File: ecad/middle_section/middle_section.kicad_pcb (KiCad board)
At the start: 2 copper layers, 12 parts, among them U1 ADS7830, U2 LM4040DBZ-3

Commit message: [WIP]
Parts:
- added J1: JST SH, Connector_JST:JST_SH_BM04B-SRSS-TB_1x04-1MP_P1.00mm_Vertical, B.Cu at (99.5, 125.6)
- added JP1: ~, Jumper:SolderJumper-3_P1.3mm_Open_RoundedPad1.0x1.5mm, B.Cu at (109.3, 129.3)
- added JP2: ~, Jumper:SolderJumper-3_P1.3mm_Open_RoundedPad1.0x1.5mm, B.Cu at (109.3, 126.8)
- C1, C3: value C_Polarized -> 2u2; footprint Capacitor_SMD:CP_Elec_4x5.7 -> Capacitor_SMD:C_0805_2012Metric; moved to B.Cu
- C2, C4: value C -> 100n; moved to B.Cu
- R1: value R -> 100; moved to B.Cu
- U1, U2: moved to B.Cu
- moved RV1 60.8 mm to (100.0, 100.0), turned to 90 degrees
- moved RV2 38.5 mm to (119.0, 100.0), turned to 90 degrees
- moved RV5 30.5 mm to (176.0, 100.0), turned to 90 degrees
- moved C1 27.8 mm to (113.2, 120.5)
- moved R1 25.1 mm to (113.2, 126.3), turned to 0 degrees
- moved C2 22.9 mm to (113.2, 118.7)
- moved C3 22.6 mm to (103.2, 121.6), turned to 90 degrees
- moved C4 22.1 mm to (105.0, 121.8), turned to 90 degrees
- moved U2 21.1 mm to (113.3, 123.5), turned to -90 degrees
- moved U1 20.9 mm to (108.6, 119.4), turned to -90 degrees
- moved RV3 16.8 mm to (138.0, 100.0), turned to 90 degrees
- moved RV4 9.94 mm to (157.0, 100.0), turned to 90 degrees
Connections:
- U1 pad 12: unconnected-(U1-A0-Pad12) -> /A1
- U1 pad 13: unconnected-(U1-A1-Pad13) -> /A0
- U1 pad 14: unconnected-(U1-SCL-Pad14) -> /SCK
- U1 pad 15: unconnected-(U1-SDA-Pad15) -> /SDA
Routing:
- net /SCK: track 0.00 -> 9.33 mm
- net +3V3: track 0.00 -> 8.92 mm
- net /SDA: track 0.00 -> 7.95 mm
- net /A0: track 0.00 -> 7.50 mm, vias 0 -> 2
- net +3V0: track 0.00 -> 7.37 mm
- net GND: track 0.00 -> 7.19 mm
- net /A1: track 0.00 -> 4.71 mm
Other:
- board outline added: 100 x 78 mm

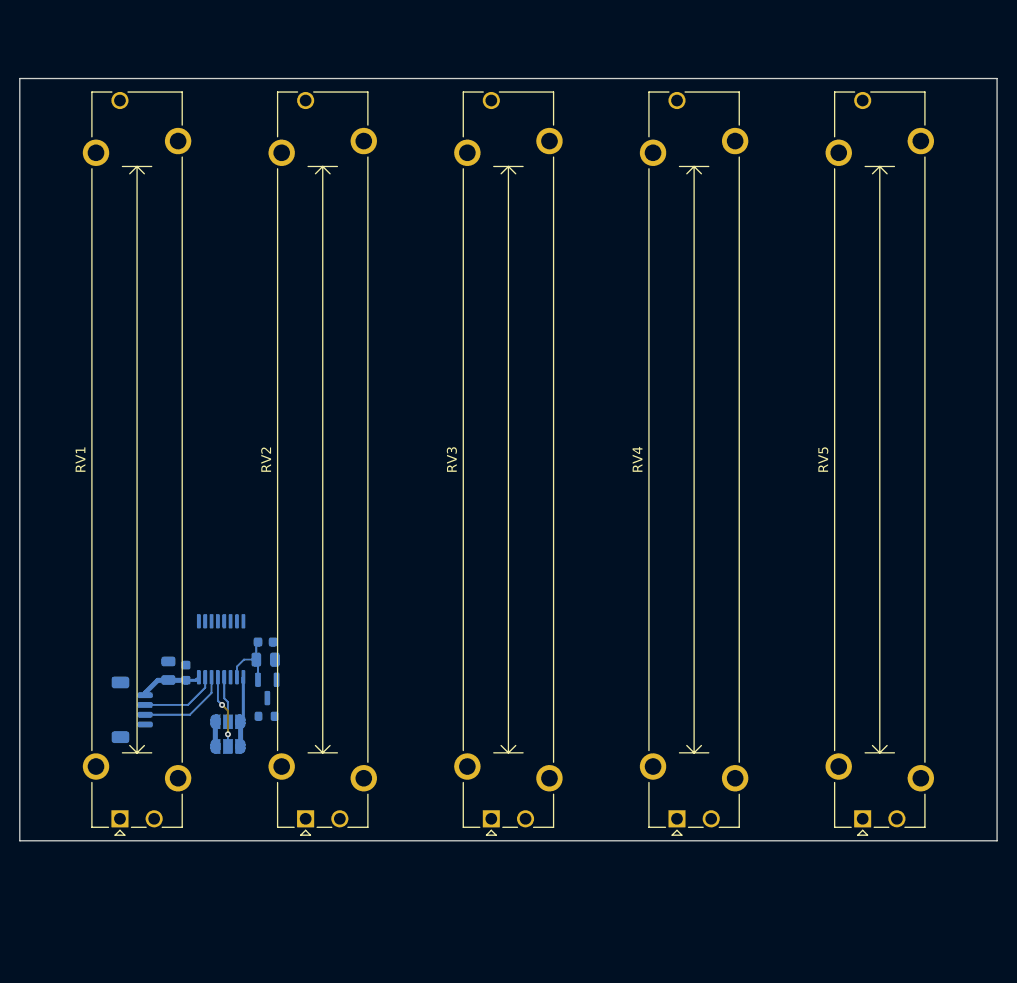
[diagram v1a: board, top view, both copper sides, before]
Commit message: Finishes up Middle Section
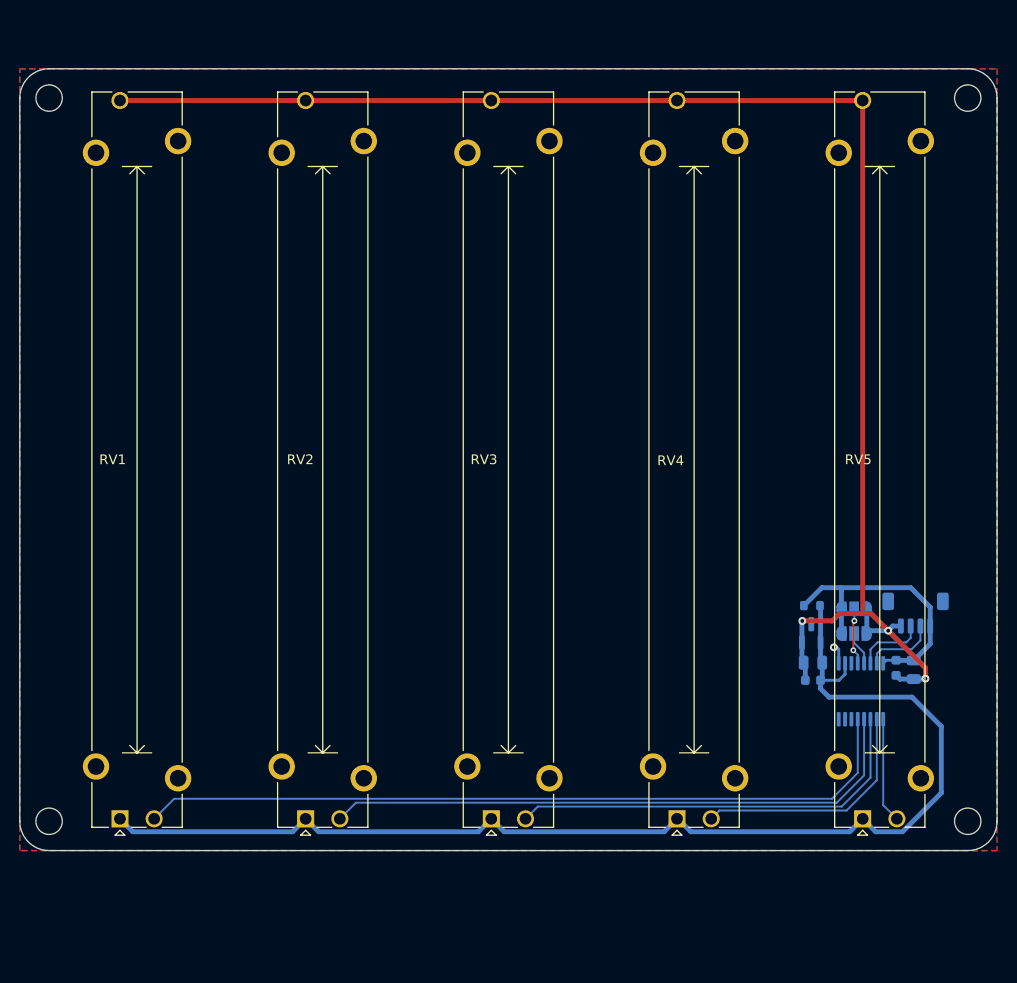
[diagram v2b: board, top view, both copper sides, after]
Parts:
- added REF**: MountingHole_2.7mm_M2.5, MountingHole:MountingHole_2.7mm_M2.5, F.Cu at (185.0, 63.0)
- added REF**: MountingHole_2.7mm_M2.5, MountingHole:MountingHole_2.7mm_M2.5, F.Cu at (91.0, 63.0)
- added REF**: MountingHole_2.7mm_M2.5, MountingHole:MountingHole_2.7mm_M2.5, F.Cu at (185.0, 137.0)
- added REF**: MountingHole_2.7mm_M2.5, MountingHole:MountingHole_2.7mm_M2.5, F.Cu at (91.0, 137.0)
- moved J1 80.8 mm to (179.7, 115.7), turned to 180 degrees
- moved C3 76.3 mm to (179.5, 121.5), turned to -90 degrees
- moved C4 72.7 mm to (177.7, 121.3), turned to -90 degrees
- moved U1 65.6 mm to (174.1, 123.7), turned to 90 degrees
- moved JP1 65.1 mm to (173.4, 117.8)
- moved JP2 65.1 mm to (173.4, 115.3)
- moved R1 56.9 mm to (169.1, 114.9)
- moved C2 56.1 mm to (169.2, 122.6), turned to 180 degrees
- moved C1 56.0 mm to (169.2, 120.8), turned to 180 degrees
- moved U2 55.9 mm to (169.0, 117.8), turned to 90 degrees
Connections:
- U1 pad 1: /CH0 -> /CH4
- U1 pad 2: /CH1 -> /CH3
- U1 pad 4: /CH3 -> /CH1
- U1 pad 5: /CH4 -> /CH0
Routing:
- net GND: track 7.19 -> 162.6 mm, vias 0 -> 4
- net +3V0: track 7.37 -> 124.0 mm
- net /CH0: track 0.00 -> 79.4 mm
- net /CH1: track 0.00 -> 61.2 mm
- net /CH2: track 0.00 -> 43.0 mm
- net /CH3: track 0.00 -> 24.8 mm
- net +3V3: track 8.92 -> 28.7 mm
- net /CH4: track 0.00 -> 10.8 mm
- net /A0: track 7.50 -> 3.47 mm, vias 2 -> 0
- net /SCK: track 9.33 -> 7.24 mm
- net /A1: track 4.71 -> 5.82 mm, vias 0 -> 2
- added copper zone on B.Cu, net GND
- added copper zone on F.Cu, net GND
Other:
- board size 100 x 78 mm -> 100 x 80 mm
- board text added: "Addr"
- board text added: "ON"

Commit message: Updates boards
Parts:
- added R2: 100, Resistor_SMD:R_0603_1608Metric, B.Cu at (169.1, 113.4)
- J1: footprint Connector_JST:JST_SH_BM04B-SRSS-TB_1x04-1MP_P1.00mm_Vertical -> woodpecker:JST_SH_BM04B-SRSS-TB_1x04-1MP_P1.00mm_Vertical
- JP1, JP2: footprint Jumper:SolderJumper-3_P1.3mm_Open_RoundedPad1.0x1.5mm -> Jumper:SolderJumper-3_P2.0mm_Open_TrianglePad1.0x1.5mm; moved to F.Cu
- moved JP1 11.7 mm to (167.8, 107.5), turned to -90 degrees
- moved JP2 11.2 mm to (165.3, 107.5), turned to -90 degrees
- moved J1 3.66 mm to (176.0, 115.7)
- moved R1 0.06 mm to (169.1, 114.9)
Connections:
- JP1 pad 1: +3V3 -> Net-(JP1-A)
- JP2 pad 1: +3V3 -> Net-(JP1-A)
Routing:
- net Net-(JP1-A): track 0.00 -> 17.6 mm, vias 0 -> 1
- net /A1: track 5.82 -> 20.4 mm, vias 2 -> 1
- net /A0: track 3.47 -> 16.9 mm, vias 0 -> 1
- net +3V3: track 28.7 -> 22.4 mm
- net /SDA: track 7.48 -> 4.15 mm
- net /SCK: track 7.24 -> 4.00 mm
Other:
- board text added: "↑ON"
- board text removed: "ON"

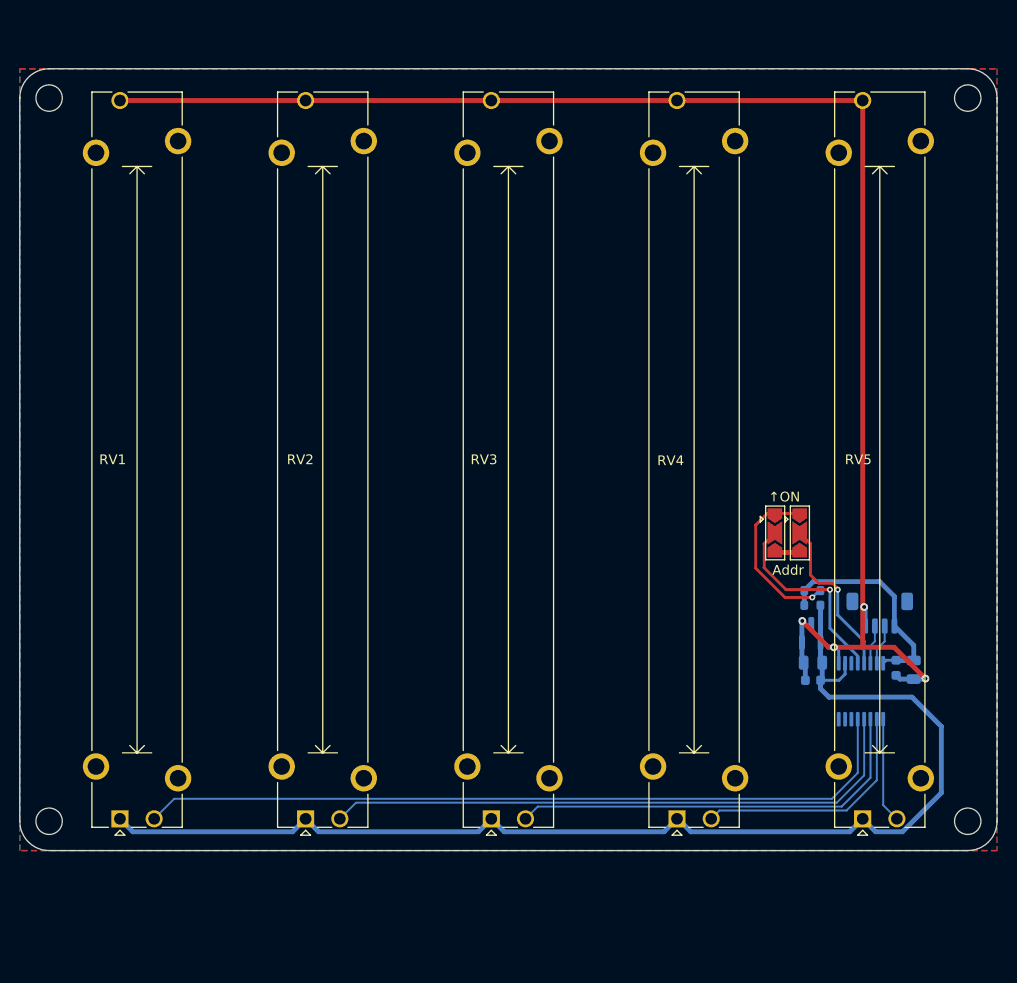
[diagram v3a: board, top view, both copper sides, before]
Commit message: Uses attiny16176
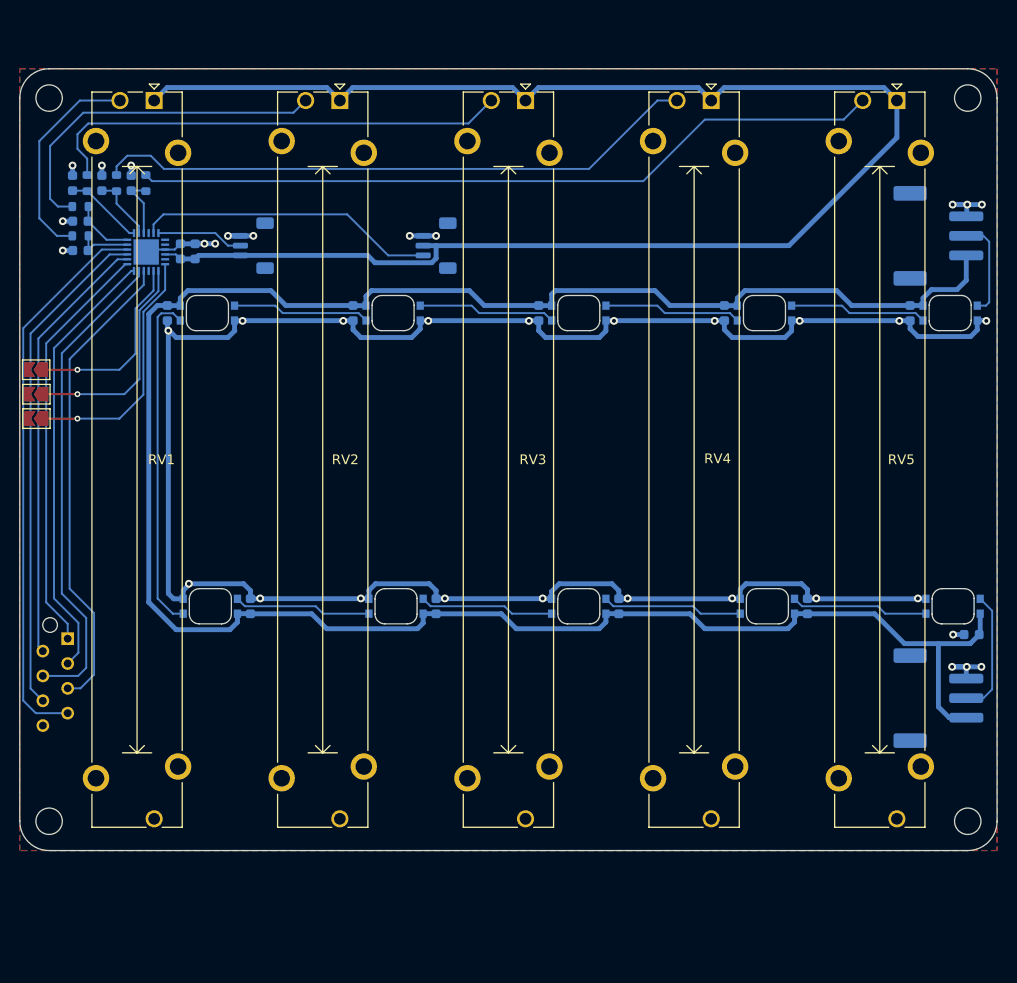
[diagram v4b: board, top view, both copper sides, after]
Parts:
- removed U2: LM4040DBZ-3, Package_TO_SOT_SMD:SOT-23
- added C10: 100n, Capacitor_SMD:C_0603_1608Metric, B.Cu at (122.1, 85.0)
- added C11: 100n, Capacitor_SMD:C_0603_1608Metric, B.Cu at (130.6, 115.0)
- added C12: 100n, Capacitor_SMD:C_0603_1608Metric, B.Cu at (141.1, 85.0)
- added C13: 100n, Capacitor_SMD:C_0603_1608Metric, B.Cu at (149.3, 115.0)
- added C14: 100n, Capacitor_SMD:C_0603_1608Metric, B.Cu at (160.1, 85.0)
- added C15: 100n, Capacitor_SMD:C_0603_1608Metric, B.Cu at (168.6, 115.0)
- added C16: 100n, Capacitor_SMD:C_0603_1608Metric, B.Cu at (179.1, 85.0)
- added C17: 100n, Capacitor_SMD:C_0603_1608Metric, B.Cu at (185.4, 117.9)
- added C5: 10n, Capacitor_SMD:C_0603_1608Metric, B.Cu at (93.4, 71.7)
- added C6: 10n, Capacitor_SMD:C_0603_1608Metric, B.Cu at (96.4, 71.7)
- added C7: 10n, Capacitor_SMD:C_0603_1608Metric, B.Cu at (99.4, 71.7)
- added C8: 100n, Capacitor_SMD:C_0603_1608Metric, B.Cu at (103.1, 85.0)
- added C9: 100n, Capacitor_SMD:C_0603_1608Metric, B.Cu at (111.6, 115.0)
- added D1: IN-PI32TAR, woodpecker:LED_Inolux_IN-PI32TAR_PLCC4_3.2x2.8mm_P1.5mm, B.Cu at (107.5, 115.0)
- added D10: IN-PI32TAR, woodpecker:LED_Inolux_IN-PI32TAR_PLCC4_3.2x2.8mm_P1.5mm, B.Cu at (183.2, 85.0)
- added D2: IN-PI32TAR, woodpecker:LED_Inolux_IN-PI32TAR_PLCC4_3.2x2.8mm_P1.5mm, B.Cu at (107.2, 85.0)
- added D3: IN-PI32TAR, woodpecker:LED_Inolux_IN-PI32TAR_PLCC4_3.2x2.8mm_P1.5mm, B.Cu at (126.2, 85.0)
- added D4: IN-PI32TAR, woodpecker:LED_Inolux_IN-PI32TAR_PLCC4_3.2x2.8mm_P1.5mm, B.Cu at (126.5, 115.0)
- added D5: IN-PI32TAR, woodpecker:LED_Inolux_IN-PI32TAR_PLCC4_3.2x2.8mm_P1.5mm, B.Cu at (145.2, 85.0)
- added D6: IN-PI32TAR, woodpecker:LED_Inolux_IN-PI32TAR_PLCC4_3.2x2.8mm_P1.5mm, B.Cu at (145.2, 115.0)
- added D7: IN-PI32TAR, woodpecker:LED_Inolux_IN-PI32TAR_PLCC4_3.2x2.8mm_P1.5mm, B.Cu at (164.2, 85.0)
- added D8: IN-PI32TAR, woodpecker:LED_Inolux_IN-PI32TAR_PLCC4_3.2x2.8mm_P1.5mm, B.Cu at (164.5, 115.0)
- added D9: IN-PI32TAR, woodpecker:LED_Inolux_IN-PI32TAR_PLCC4_3.2x2.8mm_P1.5mm, B.Cu at (183.5, 115.0)
- added J2: JST SH, woodpecker:JST_SH_BM03B-SRSS-TB_1x03-1MP_P1.00mm_Vertical, B.Cu at (111.9, 78.1)
- added J3: JST PH, woodpecker:JST_PH_S3B-PH-SM4-TB_1x03-1MP_P2.00mm_Horizontal, B.Cu at (182.0, 77.1)
- added J4: JST PH, woodpecker:JST_PH_S3B-PH-SM4-TB_1x03-1MP_P2.00mm_Horizontal, B.Cu at (182.0, 124.4)
- added J5: Conn_01x08, Connector_TE-Connectivity:TE_Micro-MaTch_215079-8_2x04_P1.27mm_Vertical, B.Cu at (92.9, 118.3)
- added JP3: SolderJumper_2_Open, Jumper:SolderJumper-2_P1.3mm_Open_TrianglePad1.0x1.5mm, F.Cu at (89.7, 95.8)
- added R3: 100, Resistor_SMD:R_0603_1608Metric, B.Cu at (94.9, 71.7)
- added R4: 100, Resistor_SMD:R_0603_1608Metric, B.Cu at (97.9, 71.7)
- added R5: 100, Resistor_SMD:R_0603_1608Metric, B.Cu at (100.9, 71.7)
- C1: value 2u2 -> 10n; footprint Capacitor_SMD:C_0805_2012Metric -> Capacitor_SMD:C_0603_1608Metric
- C2: value 100n -> 10n
- C3: value 2u2 -> 100n; footprint Capacitor_SMD:C_0805_2012Metric -> Capacitor_SMD:C_0603_1608Metric
- C4: value 100n -> 10u
- J1: footprint woodpecker:JST_SH_BM04B-SRSS-TB_1x04-1MP_P1.00mm_Vertical -> woodpecker:JST_SH_BM03B-SRSS-TB_1x03-1MP_P1.00mm_Vertical
- JP1, JP2: value ~ -> SolderJumper_2_Open; footprint Jumper:SolderJumper-3_P2.0mm_Open_TrianglePad1.0x1.5mm -> Jumper:SolderJumper-2_P1.3mm_Open_TrianglePad1.0x1.5mm
- U1: value ADS7830 -> ATtiny1617-M; footprint Package_SO:TSSOP-16_4.4x5mm_P0.65mm -> Package_DFN_QFN:QFN-24-1EP_4x4mm_P0.5mm_EP2.6x2.6mm
- moved C2 88.5 mm to (94.2, 75.6)
- moved C3 86.4 mm to (104.4, 78.7), turned to 90 degrees
- moved C1 86.0 mm to (94.2, 78.6)
- moved U1 85.8 mm to (100.9, 78.8), turned to 180 degrees
- moved R2 84.6 mm to (94.2, 74.1)
- moved R1 83.9 mm to (94.2, 77.1)
- moved C4 83.4 mm to (105.9, 78.7), turned to 90 degrees
- moved JP1 79.9 mm to (89.7, 90.8), turned to 180 degrees
- moved JP2 76.9 mm to (89.7, 93.3), turned to 180 degrees
- moved J1 58.9 mm to (130.6, 78.1), turned to 90 degrees
- turned RV1 to -90 degrees
- turned RV2 to -90 degrees
- turned RV3 to -90 degrees
- turned RV4 to -90 degrees
- turned RV5 to -90 degrees
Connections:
- C1 pad 1: +3V0 -> /CH0
- C2 pad 1: +3V0 -> /CH1
- J1 pad 1: +3V3 -> /UDPI
- J1 pad 2: /SDA -> +3V3
- J1 pad 3: /SCK -> GND
- JP1 pad 1: Net-(JP1-A) -> /A0
- JP1 pad 2: /A0 -> GND
- JP2 pad 1: Net-(JP1-A) -> /A1
- JP2 pad 2: /A1 -> GND
- R1 pad 1: +3V3 -> /CH0_RAW
- R1 pad 2: +3V0 -> /CH0
- R2 pad 1: +3V3 -> /CH1_RAW
- R2 pad 2: Net-(JP1-A) -> /CH1
- RV1 pad 1: +3V0 -> +3V3
- RV1 pad 2: /CH0 -> /CH0_RAW
- RV2 pad 1: +3V0 -> +3V3
- RV2 pad 2: /CH1 -> /CH1_RAW
- RV3 pad 1: +3V0 -> +3V3
- RV3 pad 2: /CH2 -> /CH2_RAW
- RV4 pad 1: +3V0 -> +3V3
- RV4 pad 2: /CH3 -> /CH3_RAW
- RV5 pad 1: +3V0 -> +3V3
- RV5 pad 2: /CH4 -> /CH4_RAW
- U1 pad 1: /CH4 -> unconnected-(U1-PA2-Pad1)
- U1 pad 10: +3V0 -> /COL5
- U1 pad 11: unconnected-(U1-COM-Pad11) -> /COL4
- U1 pad 12: /A1 -> /COL3
- U1 pad 13: /A0 -> /COL1
- U1 pad 14: /SCK -> /COL2
- U1 pad 15: /SDA -> /R6_SW
- U1 pad 16: +3V3 -> /R5_SW
- U1 pad 2: /CH3 -> unconnected-(U1-PA3-Pad2)
- U1 pad 3: /CH2 -> GND
- U1 pad 4: /CH1 -> +3V3
- U1 pad 5: /CH0 -> unconnected-(U1-PA4-Pad5)
- U1 pad 6: unconnected-(U1-CH5-Pad6) -> /A2
- U1 pad 7: unconnected-(U1-CH6-Pad7) -> /A1
- U1 pad 8: unconnected-(U1-CH7-Pad8) -> /A0
- U1 pad 9: GND -> unconnected-(U1-PB7-Pad9)
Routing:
- net +5V: track 0.00 -> 231.2 mm
- net +3V3: track 22.4 -> 167.1 mm
- net +3V0: track 124.0 -> 0.00 mm
- net GND: track 163.0 -> 242.2 mm, vias 4 -> 37
- net /CH4_RAW: track 0.00 -> 77.0 mm
- net /CH0: track 79.4 -> 5.79 mm
- net /CH3_RAW: track 0.00 -> 62.1 mm
- net /R5_SW: track 0.00 -> 57.2 mm
- net /CH1: track 61.2 -> 6.33 mm
- net /R6_SW: track 0.00 -> 51.3 mm
- net /COL4: track 0.00 -> 49.7 mm
- net /COL5: track 0.00 -> 48.8 mm
- net /CH2_RAW: track 0.00 -> 48.4 mm
- net /COL3: track 0.00 -> 45.2 mm
- net /COL2: track 0.00 -> 44.6 mm
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- removed copper zone on B.Cu, net GND
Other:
- board text removed: "Addr"
- board text removed: "↑ON"

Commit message: [WIP] Control board
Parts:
- removed C10, C11, C12, C13, C14, C15, C16, C17, C8, C9: 100n, Capacitor_SMD:C_0603_1608Metric
- removed D1, D10, D2, D3, D4, D5, D6, D7, D8, D9: IN-PI32TAR, woodpecker:LED_Inolux_IN-PI32TAR_PLCC4_3.2x2.8mm_P1.5mm
- removed J3, J4: JST PH, woodpecker:JST_PH_S3B-PH-SM4-TB_1x03-1MP_P2.00mm_Horizontal
- moved JP1 99.7 mm to (186.1, 116.0), turned to 0 degrees
- moved JP2 99.7 mm to (186.1, 118.5), turned to 0 degrees
- moved JP3 99.7 mm to (186.1, 121.0), turned to 0 degrees
- moved C3 26.7 mm to (130.6, 84.1)
- moved C4 26.7 mm to (132.1, 84.1)
- moved J1 26.7 mm to (156.8, 83.5)
- moved C1 26.7 mm to (120.4, 84.0)
- moved C2 26.7 mm to (120.4, 81.0)
- moved R1 26.7 mm to (120.4, 82.5)
- moved R2 26.7 mm to (120.4, 79.5)
- moved U1 26.7 mm to (127.1, 84.2)
- moved C5 26.7 mm to (119.6, 77.1)
- moved C6 26.7 mm to (122.6, 77.1)
- moved C7 26.7 mm to (125.6, 77.1)
- moved R3 26.7 mm to (121.1, 77.1)
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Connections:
- U1 pad 6: /A2 -> /A0
- U1 pad 8: /A0 -> /A2
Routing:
- net +5V: track 231.2 -> 0.00 mm
- net GND: track 242.2 -> 19.1 mm, vias 37 -> 11
- net /A2: track 25.5 -> 83.1 mm
- net /A0: track 19.4 -> 76.9 mm
- net /A1: track 22.3 -> 79.5 mm
- net Net-(D1-DIN): track 34.9 -> 0.00 mm
- net /CH2_RAW: track 48.4 -> 26.4 mm
- net /CH3_RAW: track 62.1 -> 41.5 mm
- net +3V3: track 167.1 -> 147.6 mm
- net /CH4_RAW: track 77.0 -> 57.6 mm
- net /CH1_RAW: track 36.1 -> 18.0 mm
- net Net-(D6-DOUT): track 14.4 -> 0.00 mm
- net Net-(D5-DIN): track 14.1 -> 0.00 mm
- net Net-(D3-DIN): track 14.1 -> 0.00 mm
- net Net-(D10-DOUT): track 14.1 -> 0.00 mm
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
